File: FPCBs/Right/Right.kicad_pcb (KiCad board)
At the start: 2 copper layers, 70.8 x 80.4 mm, 22 parts, among them J1 PCB, J5 2nd Focus+Shutter, J6 FPC Focus/Shutter, SW1 Mode Dial, SW2 ON/OFF, SW3 Focus+Shutter, SW4 Focus+Shutter 2, U1 SG-105, U2 SG-105

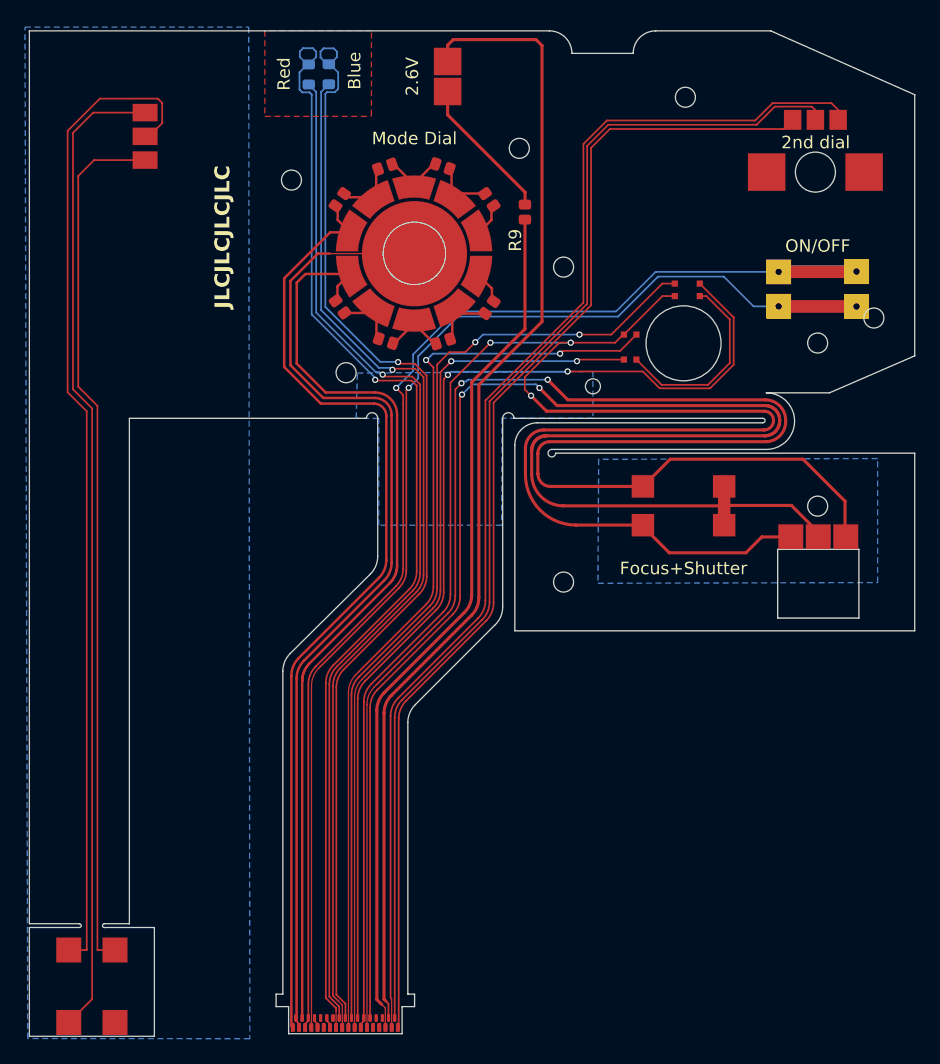
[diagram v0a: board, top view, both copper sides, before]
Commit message: Add 1st dial connector
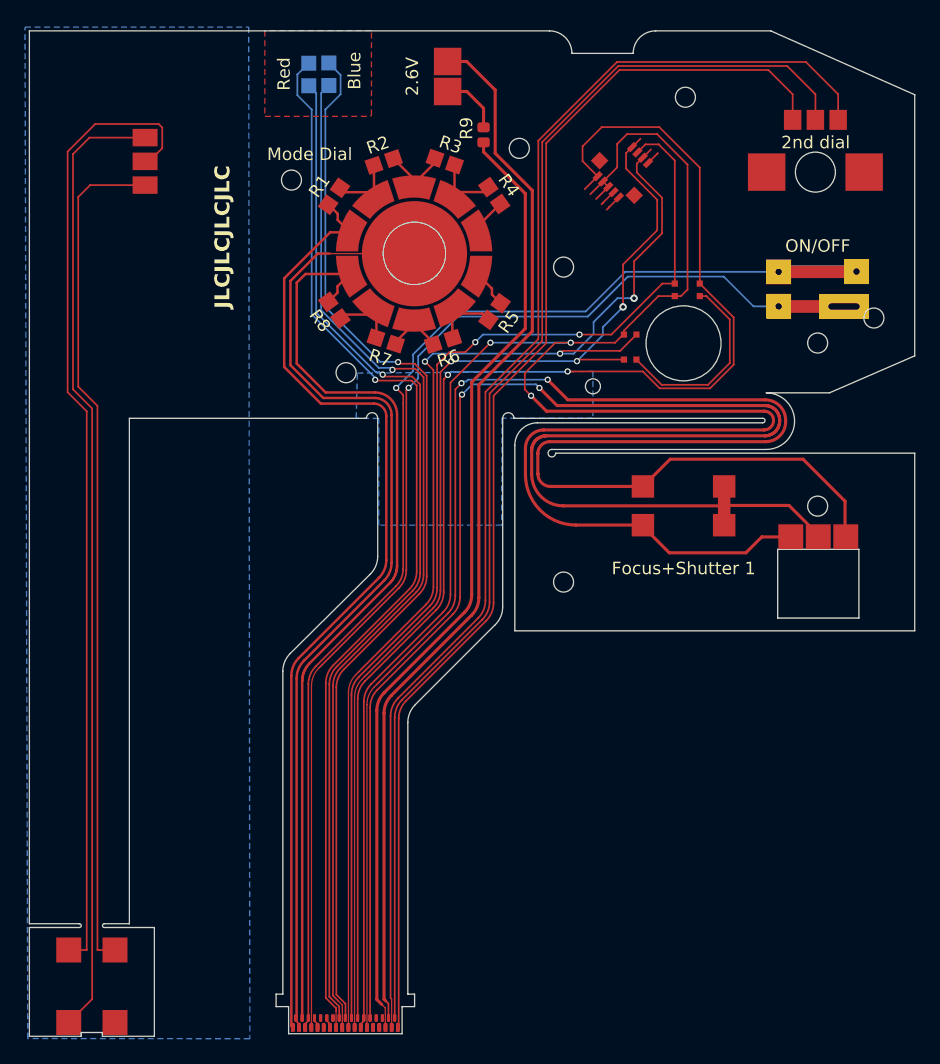
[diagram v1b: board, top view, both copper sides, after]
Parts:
- added J4: shutter+1st_dial, Leica-G9ii:Connector-2Rows-9Pins-0.60mm, F.Cu at (129.7, 111.2)
- R1, R2, R3, R4, R5, R6, R7, R8: footprint Leica-G9ii:R_2x1mm -> Leica-G9ii:R_0603
- SW3: value Focus+Shutter -> Focus+Shutter 1
- moved R9 7.01 mm to (118.5, 108.3)
- moved J6 2.00 mm to (91.4, 110.4)
- moved R1 0.53 mm to (106.5, 113.2)
- moved R5 0.53 mm to (119.4, 122.5)
- moved R8 0.52 mm to (106.6, 122.3)
- moved R4 0.52 mm to (119.3, 113.2)
- moved R3 0.42 mm to (115.4, 110.5)
- moved R2 0.40 mm to (110.5, 110.5)
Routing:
- net Net-(J1-Pin_23): track 150.3 -> 176.9 mm
- net Net-(J1-Pin_22): track 86.1 -> 111.1 mm
- net Net-(J1-Pin_19): track 74.1 -> 96.6 mm, vias 2 -> 3
- net Net-(J1-Pin_21): track 70.2 -> 92.1 mm, vias 2 -> 3
- net Net-(J1-Pin_20): track 76.6 -> 90.3 mm
- net Net-(J1-Pin_31): track 69.6 -> 77.2 mm
- net Net-(BT1--): track 92.2 -> 85.1 mm
- net Net-(J1-Pin_35): track 93.6 -> 100.4 mm
- net Net-(BT1-+): track 11.7 -> 5.00 mm
- net Net-(J1-Pin_34): track 97.1 -> 102.9 mm
- net Net-(J1-Pin_33): track 99.7 -> 105.4 mm
- net Net-(D2-K): track 89.7 -> 85.4 mm
- net Net-(D1-K): track 90.5 -> 86.5 mm
- net Net-(J6-Pin_1): track 78.9 -> 77.1 mm
- net Net-(J6-Pin_3): track 69.5 -> 67.7 mm
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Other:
- outline, holes or cut-outs redrawn

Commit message: Generate Gerbers
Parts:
- R9: footprint Leica-G9ii:R_2x1mm -> Leica-G9ii:R_0603
- moved R9 0.22 mm to (118.3, 108.2)
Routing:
- net Net-(J1-Pin_22): track 111.1 -> 111.6 mm
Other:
- board text added: "+"
- board text added: "-"

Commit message: Add engravings
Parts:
- removed J4: shutter+1st_dial, Leica-G9ii:Connector-2Rows-9Pins-0.60mm
- removed J5: 2nd Focus+Shutter, Leica-G9ii:Connector-Springs-3Pins
- removed J6: FPC Focus/Shutter, Leica-G9ii:FPC-Springs-3Pins
- removed SW4: Focus+Shutter 2, Leica-G9ii:Shutter_Olympus
- BT1: moved to B.Cu
- SW3: value Focus+Shutter 1 -> Focus+Shutter
- moved R9 2.47 mm to (120.8, 107.9)
- moved BT1 1.24 mm to (117.1, 103.8), turned to 90 degrees
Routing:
- net Net-(J6-Pin_2): track 78.0 -> 0.00 mm
- net Net-(J6-Pin_1): track 77.1 -> 0.00 mm
- net Net-(J6-Pin_3): track 67.7 -> 0.00 mm
- net Net-(J1-Pin_23): track 176.8 -> 137.9 mm
- net Net-(J1-Pin_22): track 111.6 -> 86.5 mm
- net Net-(J1-Pin_25): track 136.7 -> 113.9 mm
- net Net-(J1-Pin_19): track 96.9 -> 74.5 mm, vias 3 -> 2
- net Net-(J1-Pin_21): track 92.1 -> 70.2 mm, vias 3 -> 2
- net Net-(J1-Pin_20): track 90.3 -> 76.6 mm
- net Net-(J1-Pin_26): track 133.1 -> 123.0 mm
- net Net-(BT1-+): track 4.58 -> 10.9 mm, vias 0 -> 1
- net Net-(D1-K): track 86.5 -> 88.6 mm
- net Net-(D1-A): track 82.9 -> 84.9 mm
- net Net-(D2-K): track 85.4 -> 87.0 mm
- net Net-(D2-A): track 83.9 -> 85.4 mm
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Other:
- board size 70.8 x 80.4 mm -> 53.4 x 77.1 mm

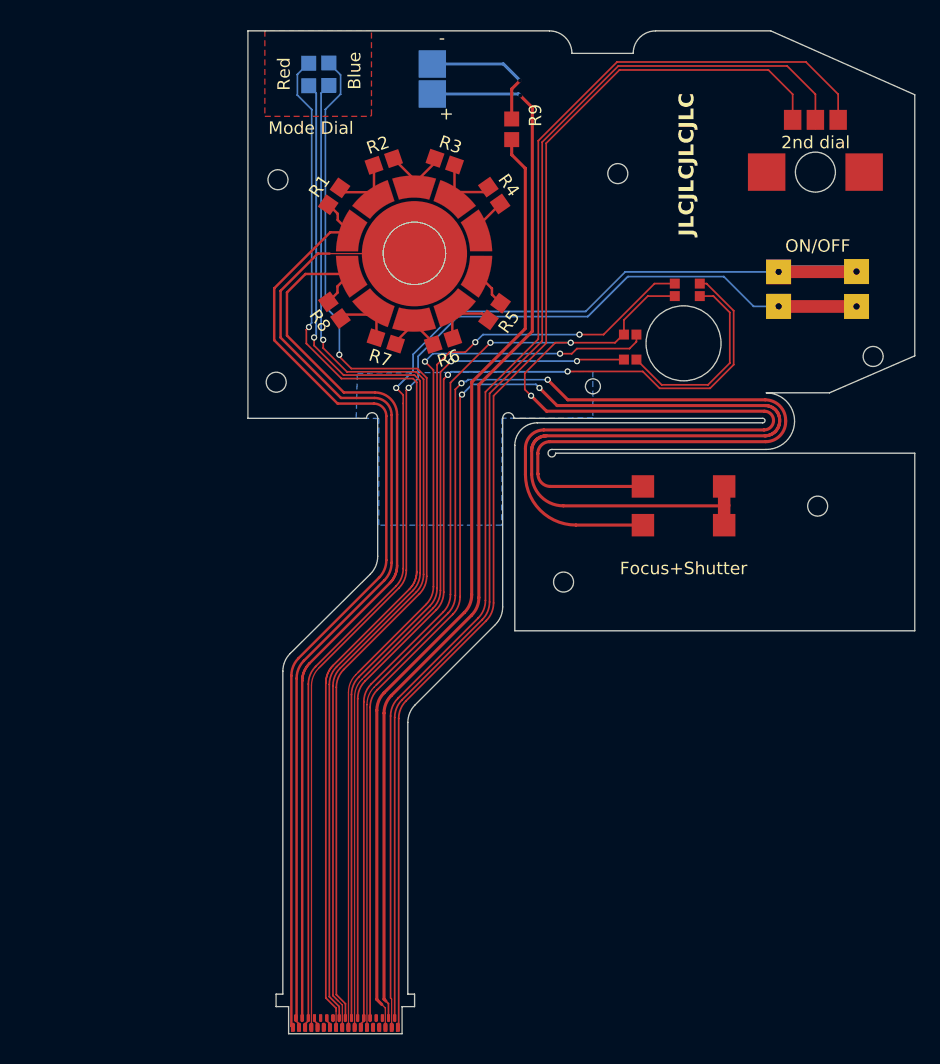
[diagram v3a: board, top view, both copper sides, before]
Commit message: Add second shutter
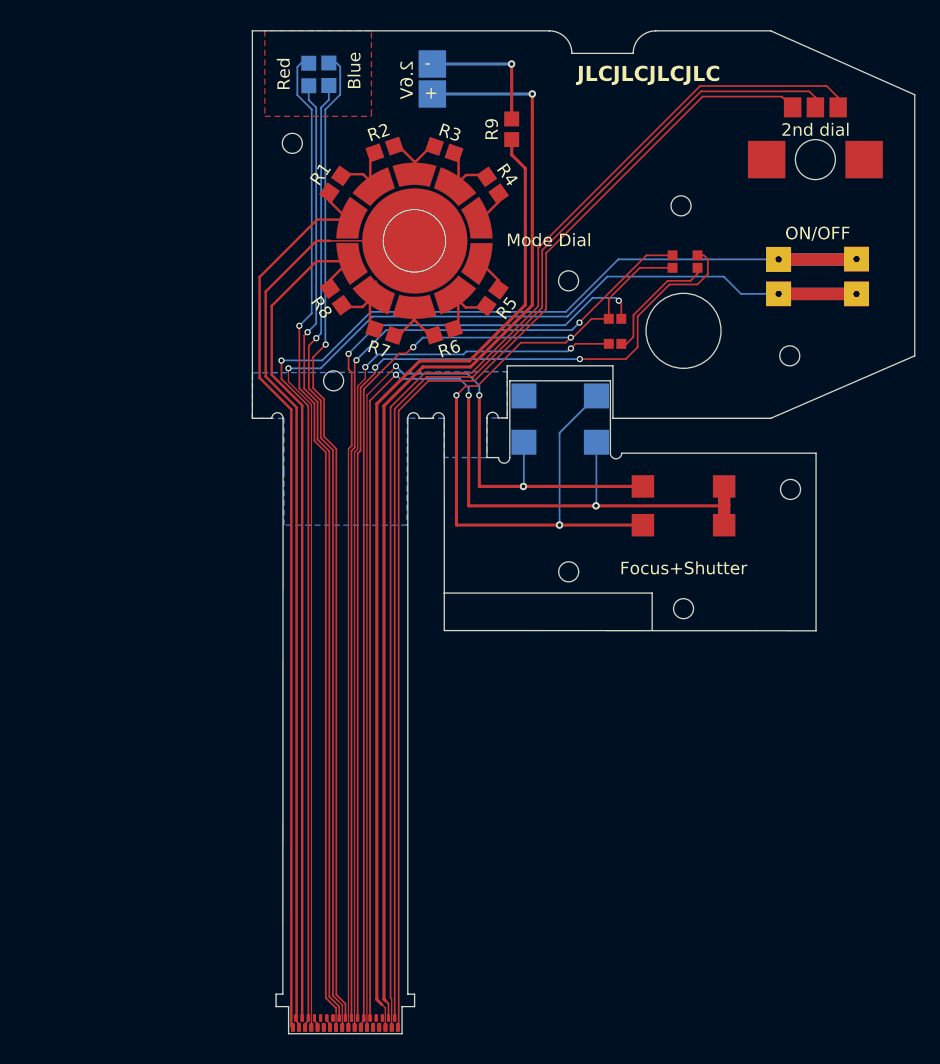
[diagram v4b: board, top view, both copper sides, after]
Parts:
- added SW4: Focus+Shutter, Leica-G9ii:Shutter_Olympus, B.Cu at (124.6, 131.1)
- moved U2 2.27 mm to (134.6, 118.5)
- moved U1 1.75 mm to (129.0, 124.0)
- moved R5 1.12 mm to (119.2, 121.3)
- moved R8 1.07 mm to (106.7, 121.3)
- moved SW1 1.02 mm to (113.0, 116.8)
- moved R2 1.00 mm to (110.6, 109.5)
- moved RV1 1.00 mm to (145.1, 110.3)
- moved SW2 1.00 mm to (145.2, 116.8)
- moved R1 0.97 mm to (106.6, 112.3)
- moved R3 0.95 mm to (115.3, 109.5)
- moved R4 0.83 mm to (119.2, 112.3)
- moved R6 0.75 mm to (115.3, 124.1)
- moved R7 0.70 mm to (110.6, 124.1)
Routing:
- net Net-(J1-Pin_25): track 113.9 -> 85.9 mm, vias 2 -> 3
- net Net-(J1-Pin_26): track 123.0 -> 96.7 mm, vias 2 -> 3
- net Net-(J1-Pin_23): track 137.9 -> 128.8 mm, vias 3 -> 4
- net Net-(D1-A): track 84.9 -> 76.4 mm
- net Net-(D1-K): track 88.6 -> 80.2 mm
- net Net-(D2-A): track 85.4 -> 77.1 mm
- net Net-(D2-K): track 87.0 -> 79.0 mm
- net Net-(J1-Pin_5): track 102.1 -> 109.8 mm
- net Net-(J1-Pin_7): track 102.1 -> 108.8 mm
- net Net-(J1-Pin_34): track 102.9 -> 96.6 mm
- net Net-(J1-Pin_4): track 74.9 -> 68.7 mm
- net Net-(J1-Pin_35): track 100.4 -> 94.2 mm
- net Net-(U1-K): track 16.0 -> 9.92 mm
- net Net-(J1-Pin_2): track 76.0 -> 70.0 mm
- net Net-(J1-Pin_33): track 105.4 -> 100.0 mm
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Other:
- board size 53.4 x 77.1 mm -> 53 x 77.1 mm

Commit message: Fix left fpcb
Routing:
- net Net-(R2-Pad2): track 5.17 -> 4.30 mm
- net Net-(J1-Pin_1): track 73.3 -> 72.5 mm

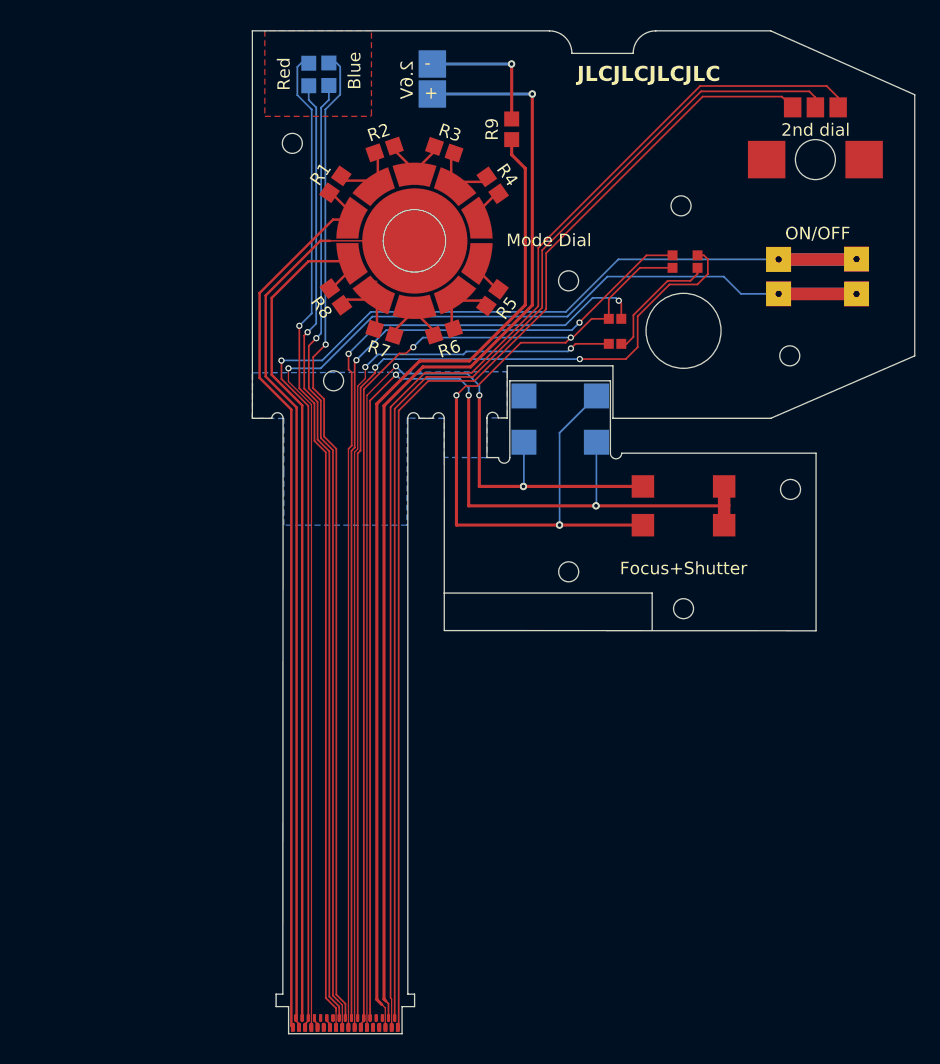
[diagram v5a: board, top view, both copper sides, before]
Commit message: Add second power button
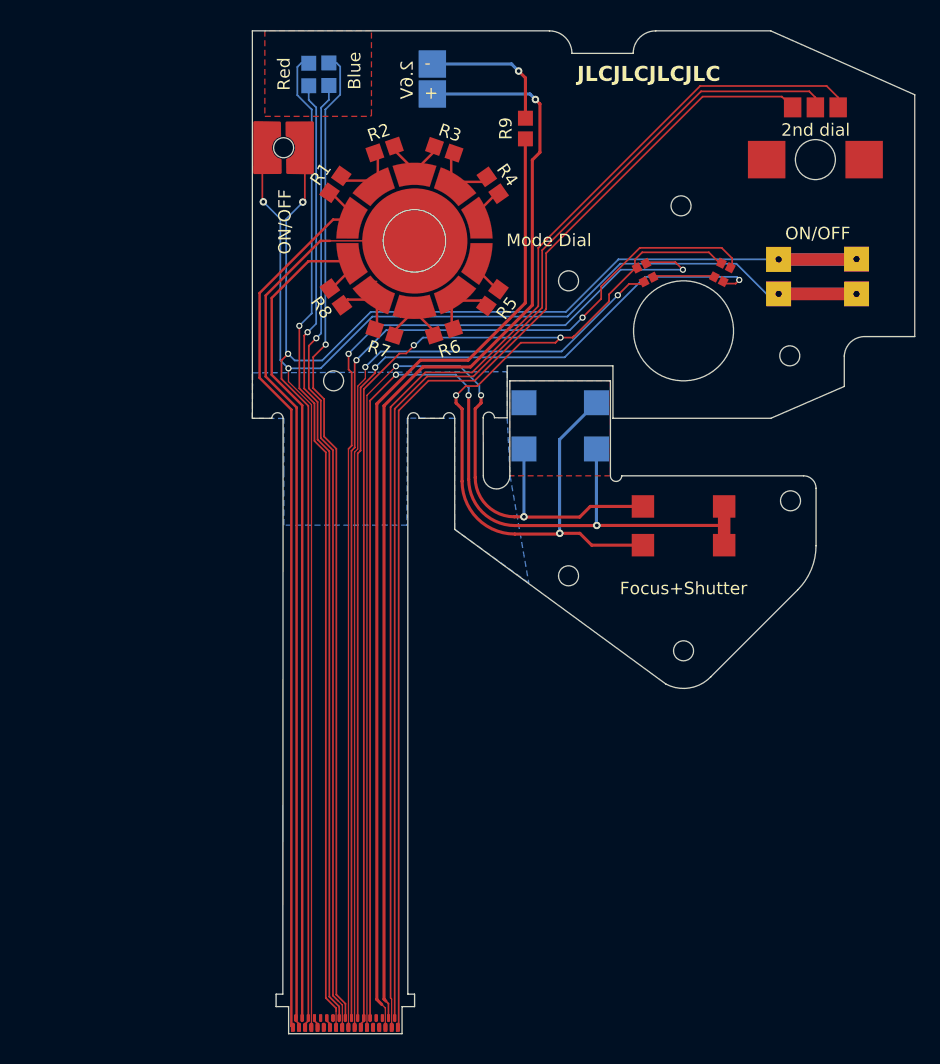
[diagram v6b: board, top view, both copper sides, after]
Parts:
- added ON/OFF: Conn_01x02_Pin, Leica-G9ii:Connector-Screw-2Pins, F.Cu at (102.5, 109.3)
- moved U1 5.28 mm to (131.4, 119.3), turned to 27 degrees
- moved U2 3.10 mm to (137.6, 119.3), turned to -27 degrees
- moved SW3 1.60 mm to (134.5, 139.6)
- moved R9 1.10 mm to (121.8, 107.8)
- moved SW4 0.54 mm to (124.6, 131.6)
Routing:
- net Net-(J1-Pin_7): track 108.8 -> 128.2 mm, vias 1 -> 2
- net Net-(J1-Pin_5): track 109.8 -> 127.4 mm, vias 1 -> 2
- net Net-(J1-Pin_19): track 79.4 -> 87.0 mm
- net Net-(J1-Pin_20): track 81.6 -> 88.3 mm
- net Net-(U1-K): track 9.92 -> 4.98 mm
- net Net-(J1-Pin_21): track 73.4 -> 78.3 mm
- net Net-(J1-Pin_25): track 85.9 -> 89.6 mm
- net Net-(J1-Pin_23): track 128.8 -> 132.0 mm
- net Net-(J1-Pin_26): track 96.7 -> 97.5 mm
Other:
- outline, holes or cut-outs redrawn
